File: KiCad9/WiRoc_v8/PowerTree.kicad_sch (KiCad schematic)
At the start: 0 parts

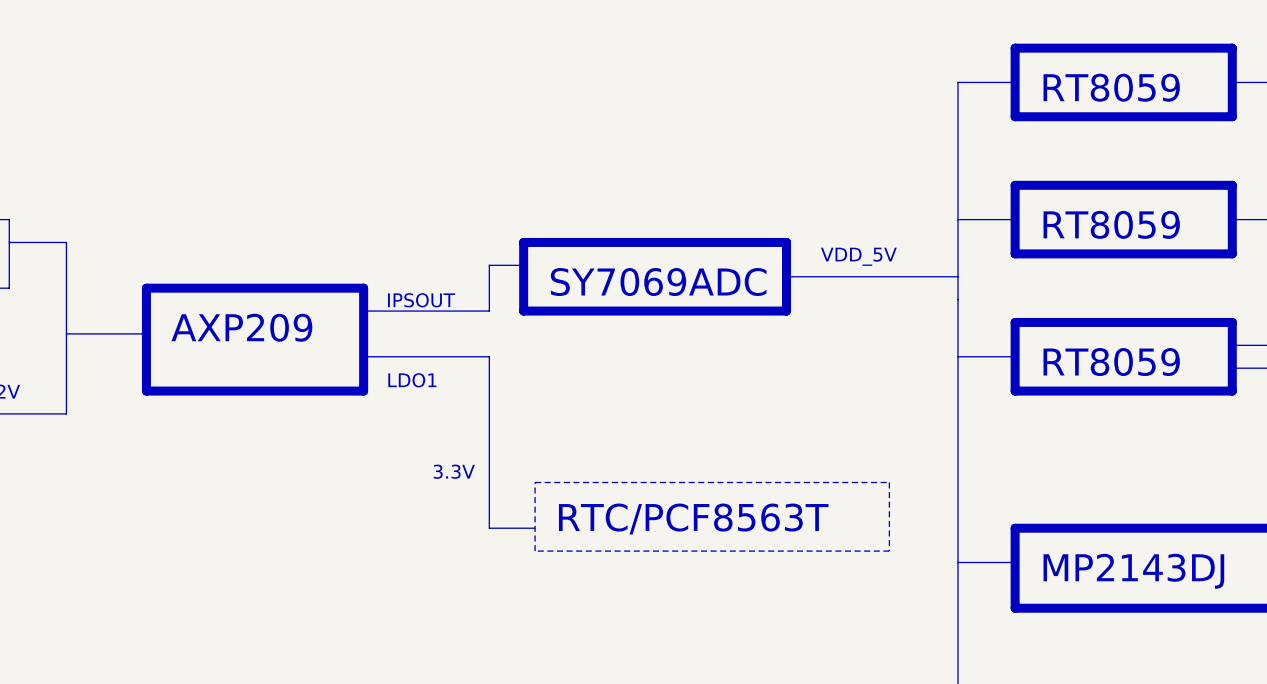
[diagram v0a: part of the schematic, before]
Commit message: change tracewidth for mem, add nettie for better length calculation
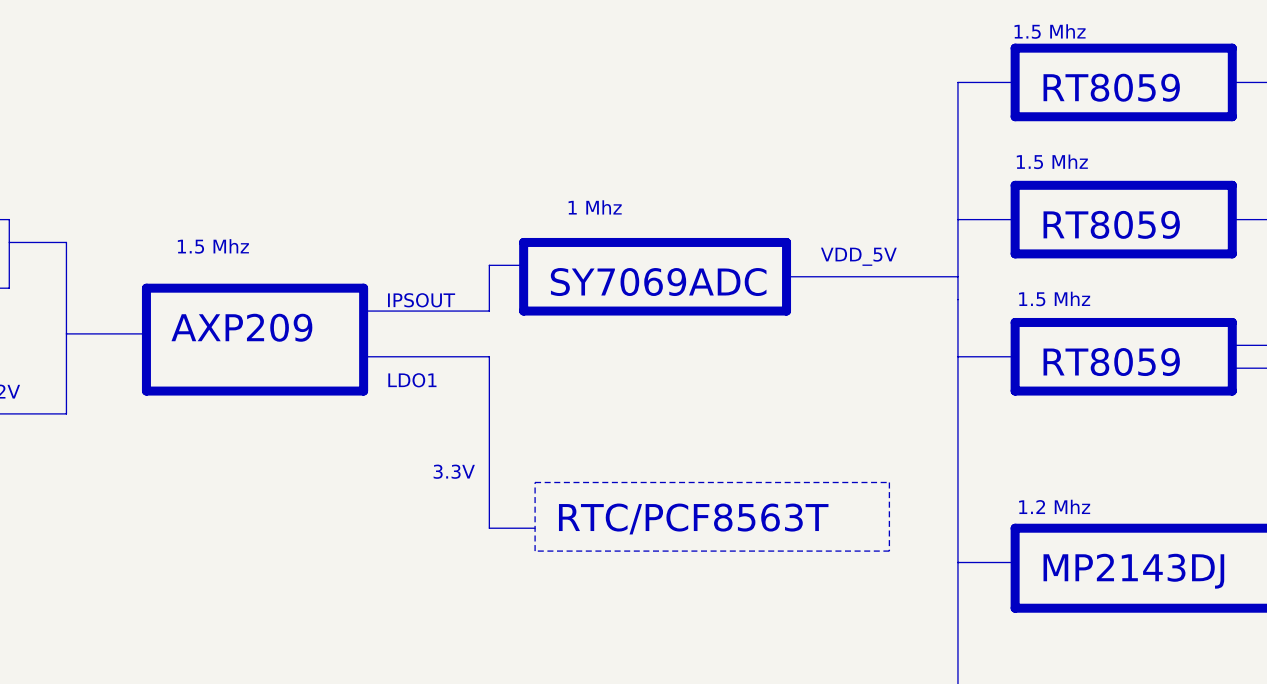
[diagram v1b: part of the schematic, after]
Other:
- note added: "1 Mhz"
- note added: "1.2 Mhz"
- note added: "1.5 Mhz"
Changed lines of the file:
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@@
 	(generator_version "9.0")
 	(paper "A4")
+	(text "1.5 Mhz"
+		(exclude_from_sim no)
+		(at 175.514 28.194 0)
+		(effects
+			(font
+				(size 1.524 1.524)
+			)
+		)
+	)
 	(text "1.5V/1A"
 		(exclude_from_sim no)
@@
 		)
 	)
+	(text "1 Mhz"
+		(exclude_from_sim no)
+		(at 124.714 33.274 0)
+		(effects
+			(font
+				(size 1.524 1.524)
+			)
+		)
+	)
 	(text "LDO2"
 		(exclude_from_sim no)
@@
 		)
 	)
+	(text "1.5 Mhz"
+		(exclude_from_sim no)
+		(at 175.26 13.716 0)
+		(effects
+			(font
+				(size 1.524 1.524)
+			)
+		)
+	)
 	(text "3.3V/200mA"
 		(exclude_from_sim no)
@@
 		)
 	)
+	(text "1.5 Mhz"
+		(exclude_from_sim no)
+		(at 175.768 43.434 0)
+		(effects
+			(font
+				(size 1.524 1.524)
+			)
+		)
+	)
+	(text "1.2 Mhz"
+		(exclude_from_sim no)
+		(at 175.768 66.548 0)
+		(effects
+			(font
+				(size 1.524 1.524)
+			)
+		)
+	)
 	(text "IPSOUT"
 		(exclude_from_sim no)
@@
 		)
 	)
+	(text "1.5 Mhz"
+		(exclude_from_sim no)
+		(at 82.296 37.592 0)
+		(effects
+			(font
+				(size 1.524 1.524)
+			)
+		)
+	)

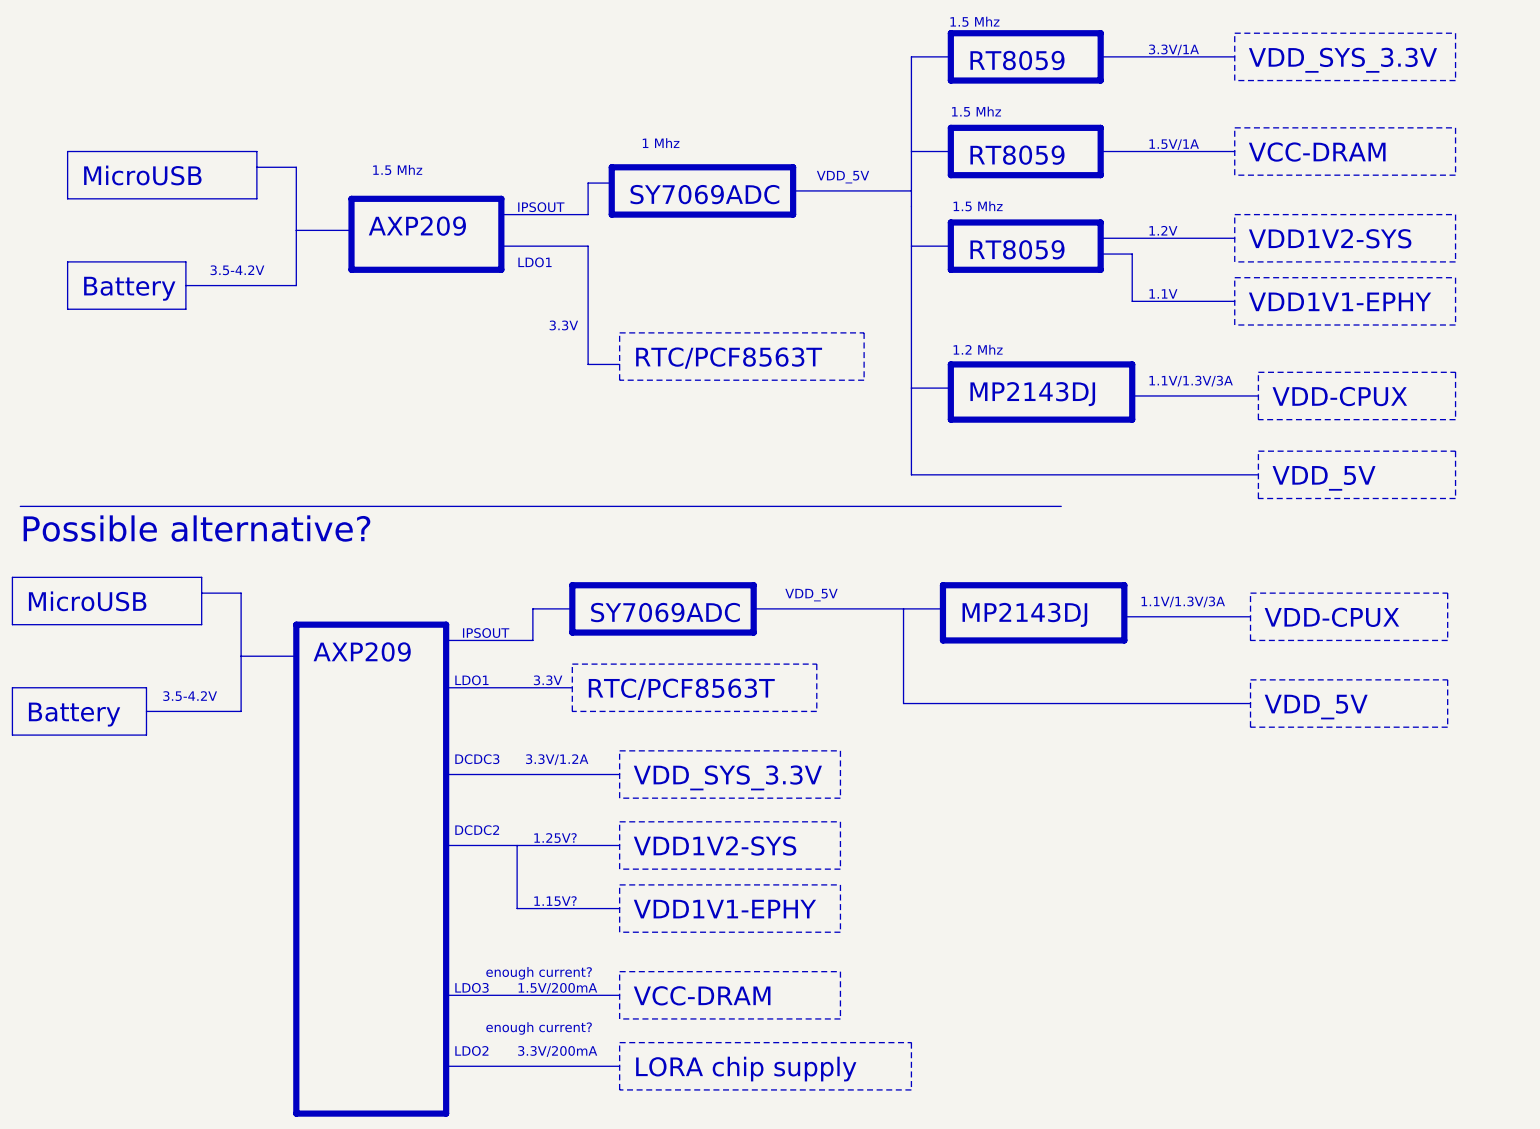
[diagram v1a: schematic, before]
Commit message: add esp32hosted-c5 board
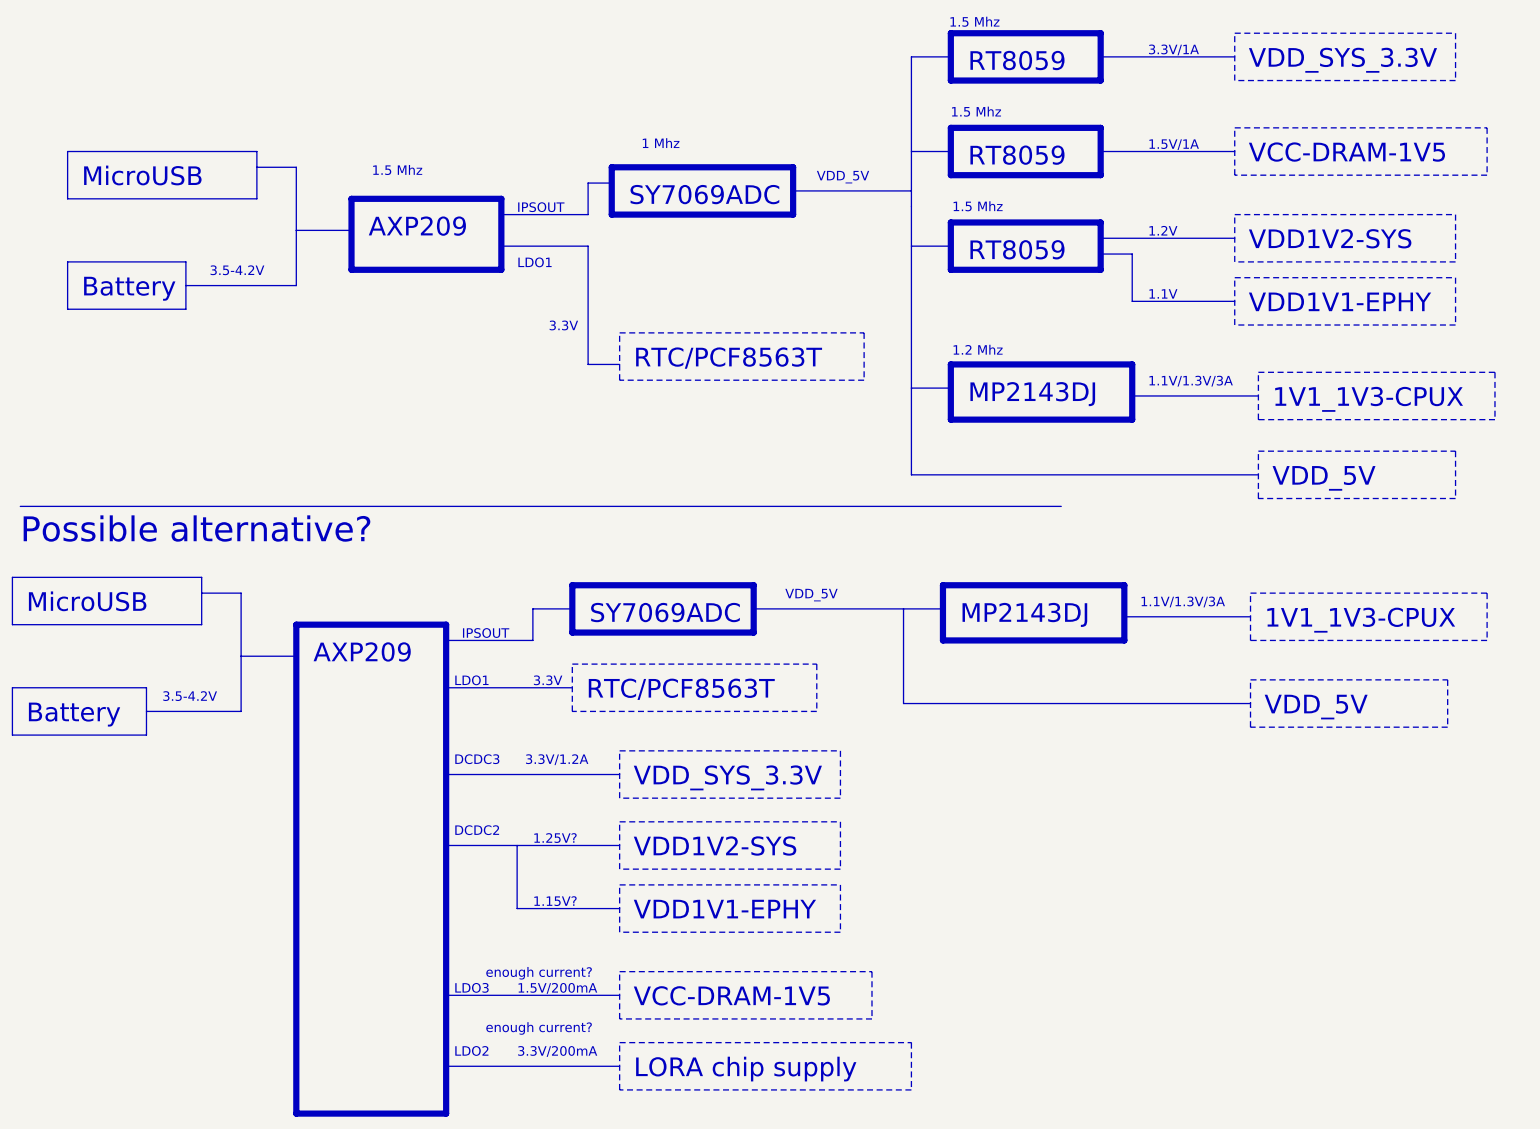
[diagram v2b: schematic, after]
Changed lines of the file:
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@@
 		)
 	)
-	(text_box "VDD-CPUX"
+	(text_box "1V1_1V3-CPUX"
 		(exclude_from_sim no)
 		(at 219.71 105.41 0)
-		(size 31.75 7.62)
-		(margins 2.25 2.25 2.25 2.25)
-		(stroke
-			(width 0)
-			(type dash)
-		)
-		(fill
-			(type none)
-		)
-		(effects
-			(font
-				(size 3 3)
-			)
-			(justify left top)
-		)
-	)
-	(text_box "VDD-CPUX"
+		(size 38.1 7.62)
+		(margins 2.25 2.25 2.25 2.25)
+		(stroke
+			(width 0)
+			(type dash)
+		)
+		(fill
+			(type none)
+		)
+		(effects
+			(font
+				(size 3 3)
+			)
+			(justify left top)
+		)
+	)
+	(text_box "1V1_1V3-CPUX"
 		(exclude_from_sim no)
 		(at 220.98 69.85 0)
-		(size 31.75 7.62)
+		(size 38.1 7.62)
 		(margins 2.25 2.25 2.25 2.25)
 		(stroke
@@
 		)
 	)
-	(text_box "VCC-DRAM"
+	(text_box "VCC-DRAM-1V5"
 		(exclude_from_sim no)
 		(at 118.11 166.37 0)
-		(size 35.56 7.62)
+		(size 40.64 7.62)
 		(margins 2.25 2.25 2.25 2.25)
 		(stroke
@@
 		)
 	)
-	(text_box "VCC-DRAM"
+	(text_box "VCC-DRAM-1V5"
 		(exclude_from_sim no)
 		(at 217.17 30.48 0)
-		(size 35.56 7.62)
-		(margins 2.25 2.25 2.25 2.25)
-		(stroke
+		(size 40.64 7.62)
+		(margins 2.25 2.25 2.25 2.25)
+		(stroke

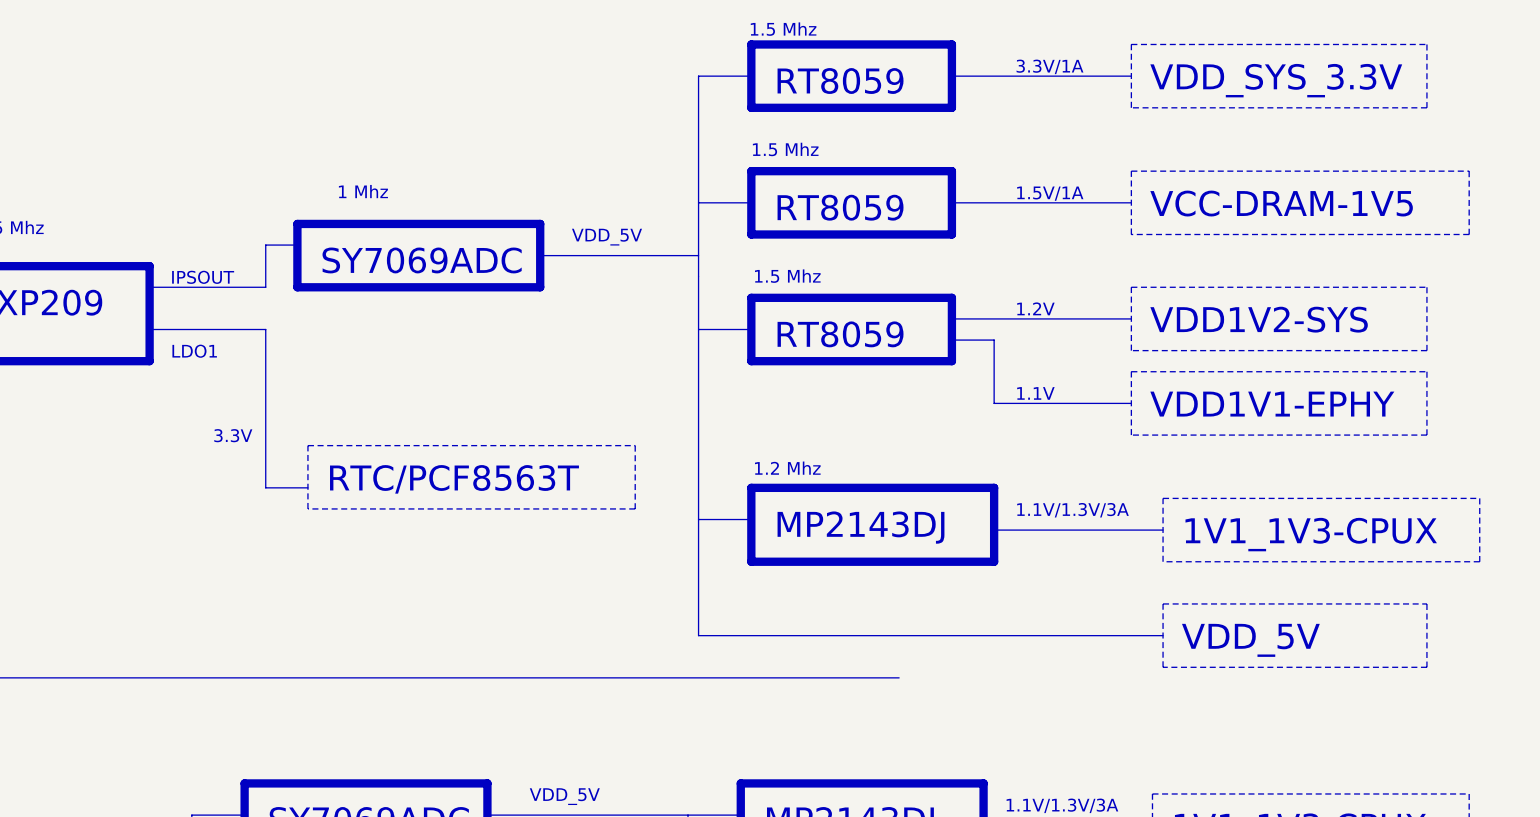
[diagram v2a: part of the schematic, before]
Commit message: change to 10uF in pdn, vdd-dram area to south caps, remove varistor, etc
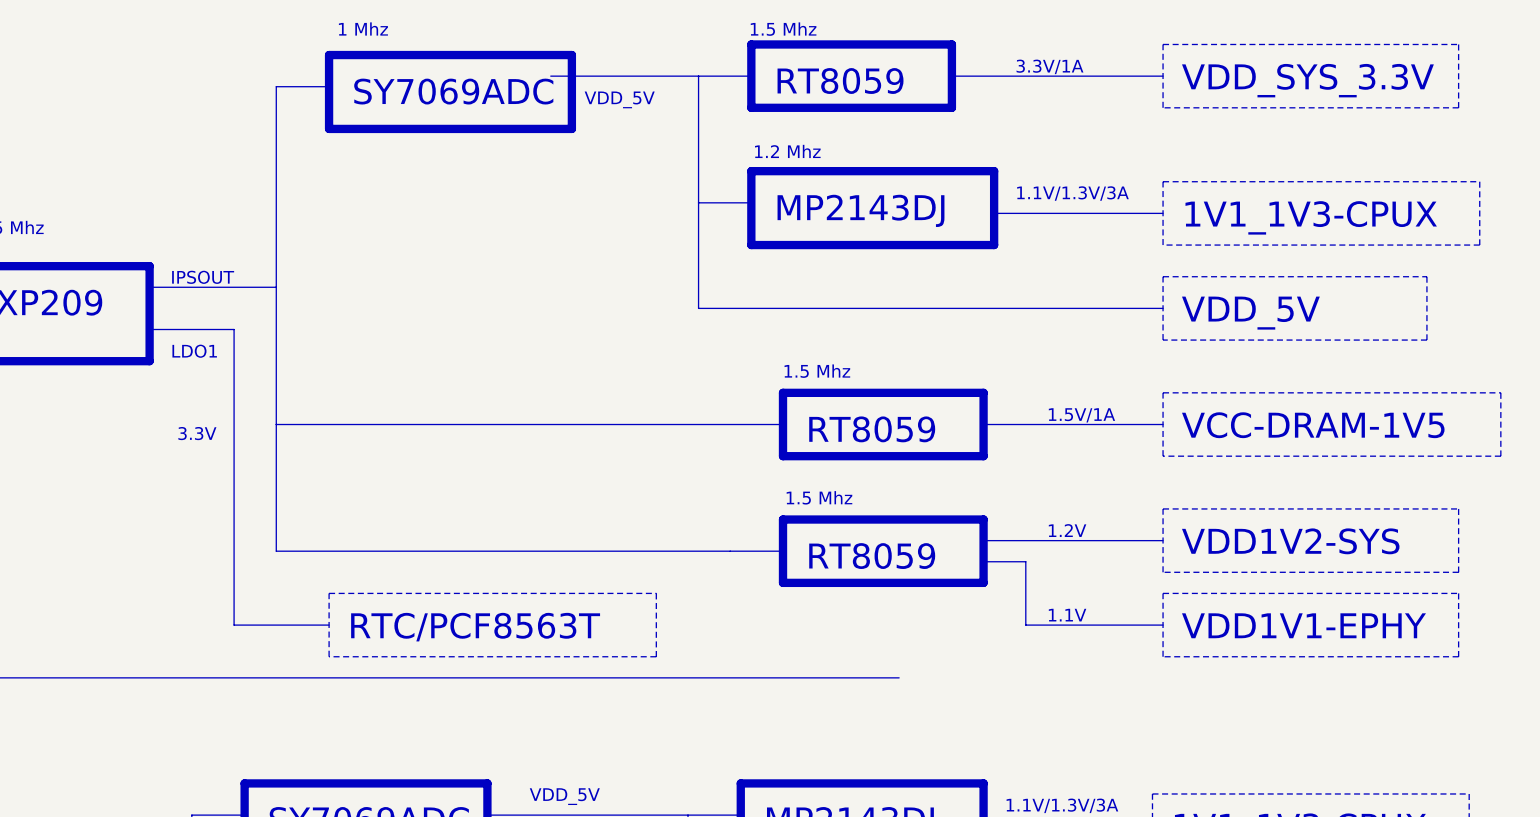
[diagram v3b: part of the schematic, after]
